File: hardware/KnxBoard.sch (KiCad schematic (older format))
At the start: 10 parts, among them J1 Conn_01x10, J1 SB, J2 KNX, J4 Conn_01x02, SW1 SW

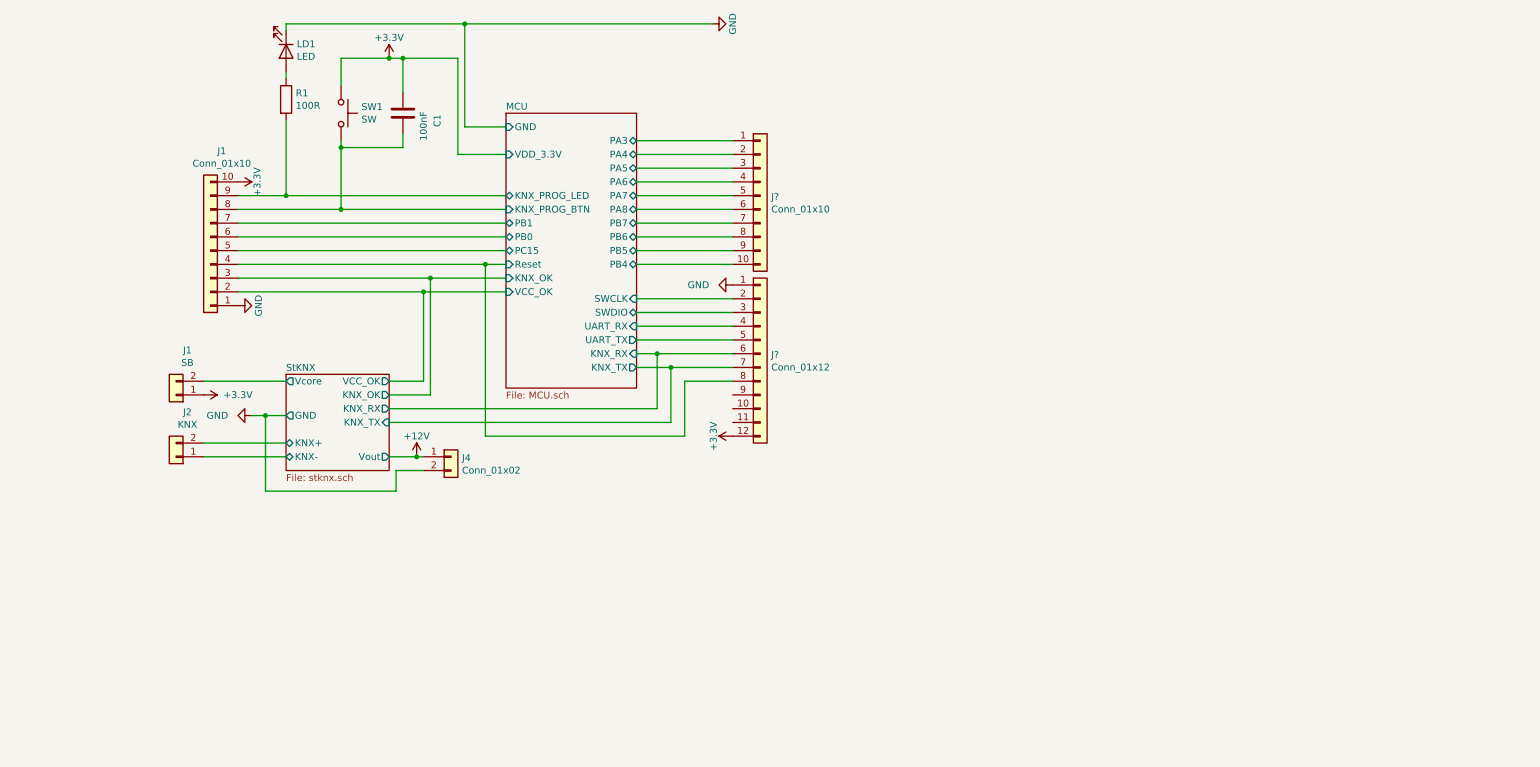
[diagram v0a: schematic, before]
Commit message: Change architecture, use NCN5130 instead STKNX
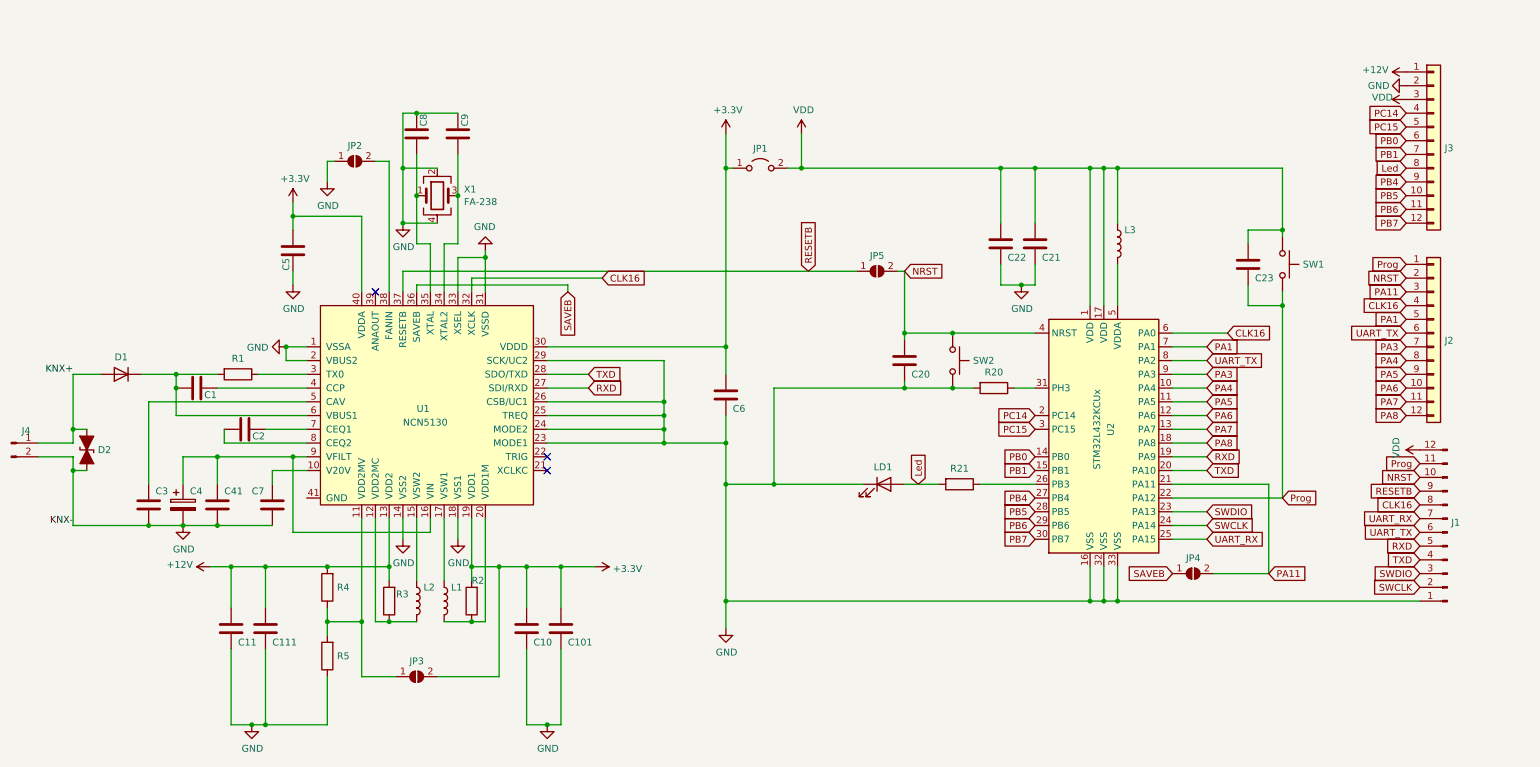
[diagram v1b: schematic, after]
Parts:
- removed J1: SB, Connector_PinHeader_2.54mm:PinHeader_1x02_P2.54mm_Vertical, symbol Connector_Generic:Conn_01x02
- removed J1: Conn_01x10, Connector_PinHeader_2.54mm:PinHeader_1x14_P2.54mm_Vertical, symbol Connector_Generic:Conn_01x10
- removed J2: KNX, stknx:KNX_Connector, symbol Connector_Generic:Conn_01x02
- removed J4: Conn_01x02, Connector_PinHeader_2.54mm:PinHeader_1x02_P2.54mm_Vertical, symbol Connector_Generic:Conn_01x02
- removed J?: Conn_01x12, Connector_FFC-FPC:Hirose_FH12-12S-0.5SH_1x12-1MP_P0.50mm_Horizontal, symbol Connector_Generic:Conn_01x12
- removed J?: Conn_01x10, symbol Connector_Generic:Conn_01x10
- added C10, C101, C11, C111, C22: 10uF 6.3V ESR < 0.1ohm, Capacitor_SMD:C_0805_2012Metric, symbol Device:C
- added C2: 220nF 50V, Capacitor_SMD:C_0603_1608Metric, symbol Device:C
- added C20, C21, C23, C5, C6: 100nF 6.3V, Capacitor_SMD:C_0402_1005Metric, symbol Device:C
- added C3: 100nF 50V, Capacitor_SMD:C_0603_1608Metric, symbol Device:C
- added C4: 100uF 35V, Capacitor_SMD:CP_Elec_6.3x7.7, symbol Device:CP
- added C41, C7: 1uF 35V ESR < 2ohm, Capacitor_SMD:C_0603_1608Metric, symbol Device:C
- added C8, C9: 10pF 6.3V, Capacitor_SMD:C_0402_1005Metric, symbol Device:C
- added D1: SS16, Diode_SMD:D_SMA, symbol Device:D
- added D2: 1SMA40CA, Diode_SMD:D_SMA, symbol Device:D_TVS_ALT
- added J1: Conn_01x12_Male, Connector_FFC-FPC:Hirose_FH12-12S-0.5SH_1x12-1MP_P0.50mm_Horizontal, symbol Connector:Conn_01x12_Male
- added J2, J3: Conn_01x12, Connector_PinHeader_2.54mm:PinHeader_1x12_P2.54mm_Vertical, symbol Connector_Generic:Conn_01x12
- added J4: Conn_01x02_Male, KnxBoard:KNX_Connector, symbol Connector:Conn_01x02_Male
- added JP1: Jumper_2_Open, Connector_PinHeader_2.54mm:PinHeader_1x02_P2.54mm_Vertical, symbol Jumper:Jumper_2_Open
- added JP2, JP3, JP4, JP5: SolderJumper_2_Open, Jumper:SolderJumper-2_P1.3mm_Open_TrianglePad1.0x1.5mm, symbol Jumper:SolderJumper_2_Open
- added L1, L2, L3: 220uH, Inductor_SMD:L_1008_2520Metric, symbol Device:L
- added R2, R3: 1R 1/16W, Resistor_SMD:R_0402_1005Metric, symbol Device:R
- added R20: 10K 1/16w, Resistor_SMD:R_0402_1005Metric, symbol Device:R
- added R21: 100R, Resistor_SMD:R_0402_1005Metric, symbol Device:R
- added R4: 67.7K 1/16w, Resistor_SMD:R_0402_1005Metric, symbol Device:R
- added R5: 590K 1/16w, Resistor_SMD:R_0402_1005Metric, symbol Device:R
- added SW2: SW_Push, Button_Switch_SMD:SW_SPST_SKQG_WithStem, symbol Switch:SW_Push
- added U1: NCN5130, Package_DFN_QFN:QFN-40-1EP_6x6mm_P0.5mm_EP4.6x4.6mm_ThermalVias, symbol KNX_NCN5130:NCN5130
- added U2: STM32L432KCUx, Package_DFN_QFN:QFN-32-1EP_5x5mm_P0.5mm_EP3.45x3.45mm, symbol MCU_ST_STM32L4:STM32L432KCUx
- added X1: FA-238, Crystal:Crystal_SMD_SeikoEpson_FA238-4Pin_3.2x2.5mm, symbol Device:Crystal_GND24
- C1: value 100nF -> 47nF 50V; Price 0.09 -> 0.085; Rating 3.3V -> (none)
- LD1: Price 0.15 -> 0.152
- R1: value 100R -> 27R 1W; footprint Resistor_SMD:R_0402_1005Metric -> Resistor_SMD:R_0612_1632Metric; Price 0.09 -> 0.382
- SW1: value SW -> SW_Push; Price 0.5 -> 0.497
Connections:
- net MCU/KNX_PROG_LED is gone; now on an unnamed net: R1.2
- net +12V: now also C11.1, C111.1, J3.1 (Pin_1), R3.2, R4.2, U1.13 (VDD2)
- net +3V3: now also C10.1, C101.1, C5.2, C6.1, JP1.1 (A), JP3.2 (B), R2.2, U1.19 (VDD1), U1.30 (VDDD), U1.40 (VDDA); no longer C1.1, SW1.1
- net GND: now also C10.2, C101.2, C11.2, C111.2, C20.2, C21.2, C22.2, C3.2, C4.2, C41.2, C5.1, C6.2, C7.2, C8.1, C9.1, D2.2 (A2), J1.1 (Pin_1), J3.2 (Pin_2), J4.2 (Pin_2), JP2.1 (A), R20.2, R5.1, SW2.2, U1.1 (VSSA), U1.14 (VSS2), U1.18 (VSS1), U1.2 (VBUS2), U1.23 (MODE1), U1.24 (MODE2), U1.25 (TREQ), U1.26 (CSB/UC1), U1.29 (SCK/UC2), U1.31 (VSSD), U1.33 (XSEL), U2.16 (VSS), U2.32 (VSS), U2.33 (VSS), X1.2, X1.4
- net at R1.1: now also U1.3 (TX0); no longer LD1.2 (A)
- net MCU/KNX_PROG_BTN: no longer names the net of C1.2
- net MCU/KNX_PROG_BTN: now also D1.1 (K), U1.6 (VBUS1); no longer SW1.2
- new net: R21.1, U2.26 (PB3)
- new net: R20.1, U2.31 (PH3)
- new net: L3.2, U2.5 (VDDA)
- new net: C7.1, U1.10 (V20V)
- new net: JP3.1 (A), R4.1, R5.2, U1.11 (VDD2MV)
- new net: L2.2, R3.1, U1.12 (VDD2MC)
- new net: L2.1, U1.15 (VSW2)
- new net: C4.1, C41.1, U1.16 (VIN), U1.9 (VFILT)
- new net: L1.1, U1.17 (VSW1)
- new net: L1.2, R2.1, U1.20 (VDD1M)
- new net: C9.2, U1.34 (XTAL2), X1.3
- new net: C8.2, U1.35 (XTAL), X1.1
- new net: JP2.2 (B), U1.38 (FANIN)
- new net: C1.1, U1.4 (CCP)
- new net: C3.1, U1.5 (CAV)
- new net: C2.1, U1.7 (CEQ1)
- new net: C2.2, U1.8 (CEQ2)
- new net CLK16: J1.8 (Pin_8), J2.4 (Pin_4), U1.32 (XCLK), U2.6 (PA0)
- new net KNX+: D1.2 (A), D2.1 (A1), J4.1 (Pin_1)
- new net Led: J3.8 (Pin_8), LD1.2 (A), R21.2
- new net NRST: C20.1, J1.10 (Pin_10), J2.2 (Pin_2), JP5.2 (B), SW2.1, U2.4 (NRST)
- new net PA1: J2.5 (Pin_5), U2.7 (PA1)
- new net PA11: J2.3 (Pin_3), JP4.2 (B), U2.21 (PA11)
- new net PA3: J2.7 (Pin_7), U2.9 (PA3)
- new net PA4: J2.8 (Pin_8), U2.10 (PA4)
- new net PA5: J2.9 (Pin_9), U2.11 (PA5)
- new net PA6: J2.10 (Pin_10), U2.12 (PA6)
- new net PA7: J2.11 (Pin_11), U2.13 (PA7)
- new net PA8: J2.12 (Pin_12), U2.18 (PA8)
- new net PB0: J3.6 (Pin_6), U2.14 (PB0)
- new net PB1: J3.7 (Pin_7), U2.15 (PB1)
- new net PB4: J3.9 (Pin_9), U2.27 (PB4)
- new net PB5: J3.10 (Pin_10), U2.28 (PB5)
- new net PB6: J3.11 (Pin_11), U2.29 (PB6)
- new net PB7: J3.12 (Pin_12), U2.30 (PB7)
- new net PC14: J3.4 (Pin_4), U2.2 (PC14)
- new net PC15: J3.5 (Pin_5), U2.3 (PC15)
- new net Prog: C23.2, J1.11 (Pin_11), J2.1 (Pin_1), SW1.2, U2.22 (PA12)
- new net RESETB: J1.9 (Pin_9), JP5.1 (A), U1.37 (RESETB)
- new net RXD: J1.5 (Pin_5), U1.27 (SDI/RXD), U2.19 (PA9)
- new net SAVEB: JP4.1 (A), U1.36 (SAVEB)
- new net SWCLK: J1.2 (Pin_2), U2.24 (PA14)
- new net SWDIO: J1.3 (Pin_3), U2.23 (PA13)
- new net TXD: J1.4 (Pin_4), U1.28 (SDO/TXD), U2.20 (PA10)
- new net UART_RX: J1.7 (Pin_7), U2.25 (PA15)
- new net UART_TX: J1.6 (Pin_6), J2.6 (Pin_6), U2.8 (PA2)
- new net VDD: C21.1, C22.1, C23.1, J1.12 (Pin_12), J3.3 (Pin_3), JP1.2 (B), L3.1, SW1.1, U2.1 (VDD), U2.17 (VDD)
- no-connect marks 0 -> 3

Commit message: KnxBoard: Continue with layer 2
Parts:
- removed C101, C111: 10uF 6.3V ESR < 0.1ohm, Capacitor_SMD:C_0805_2012Metric, symbol Device:C
- removed C7: 1uF 35V ESR < 2ohm, Capacitor_SMD:C_0603_1608Metric, symbol Device:C
- removed J1: Conn_01x12_Male, Connector_FFC-FPC:Hirose_FH12-12S-0.5SH_1x12-1MP_P0.50mm_Horizontal, symbol Connector:Conn_01x12_Male
- removed JP2, JP3, JP4, JP5: SolderJumper_2_Open, Jumper:SolderJumper-2_P1.3mm_Open_TrianglePad1.0x1.5mm, symbol Jumper:SolderJumper_2_Open
- added J1: Conn_01x10, Connector_PinHeader_1.27mm:PinHeader_2x05_P1.27mm_Vertical, symbol Connector_Generic:Conn_01x10
- added R6: NOTMOUNT, Resistor_SMD:R_0603_1608Metric, symbol Device:R
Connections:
- net RESETB is gone; now on net NRST: U1.37 (RESETB)
- net SAVEB is gone; now on net PA11: U1.36 (SAVEB)
- net +3V3: now also U1.21 (XCLKC)
- net GND: now also U1.41 (GND), J1.2 (Pin_2), R6.2
- net NRST: now also J1.3 (Pin_3)
- net RXD: now also J1.9 (Pin_9)
- net SWCLK: now also J1.6 (Pin_6)
- net SWDIO: now also J1.7 (Pin_7)
- net TXD: now also J1.8 (Pin_8)
- net UART_RX: now also J1.4 (Pin_4)
- net UART_TX: now also J1.5 (Pin_5)
- net VDD: now also J1.10 (Pin_10)
- net Vfilt: now reaches U1.10 (V20V)
- net Vfilt: now also C4.1, C41.1, U1.16 (VIN), U1.9 (VFILT)
- net CLK1: now reaches C9.2, U1.34 (XTAL2), X1.3
- net CLK0: now reaches C8.2, U1.35 (XTAL), X1.1
- net at U1.38 (FANIN): now also R6.1
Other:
- moved on the sheet: C11

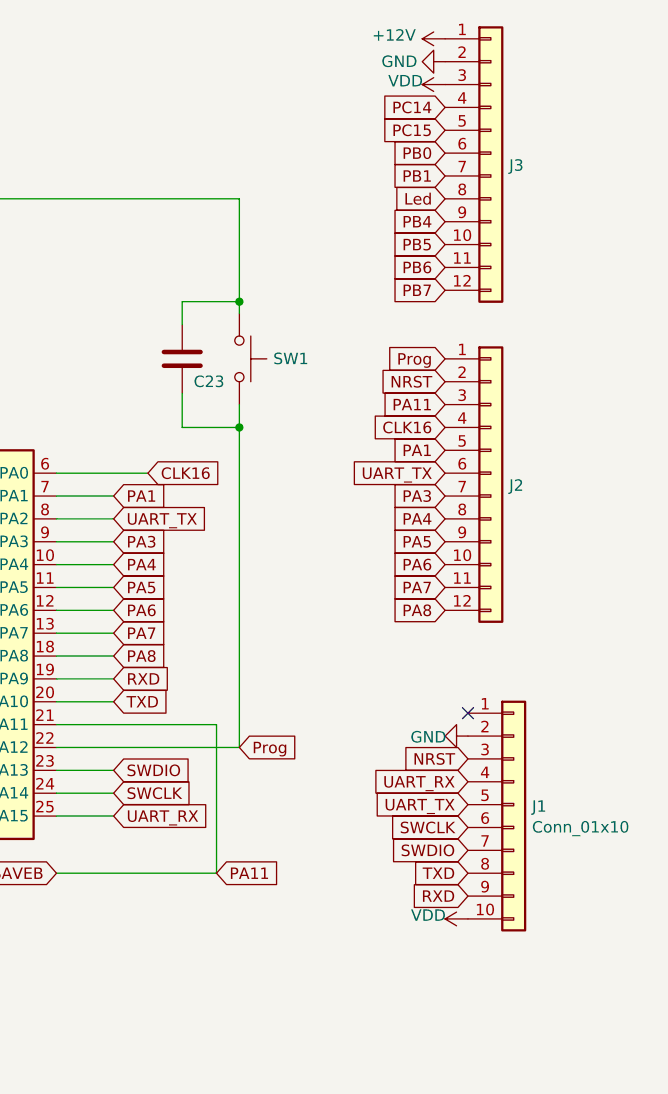
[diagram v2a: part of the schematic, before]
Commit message: Switch into 4-layers
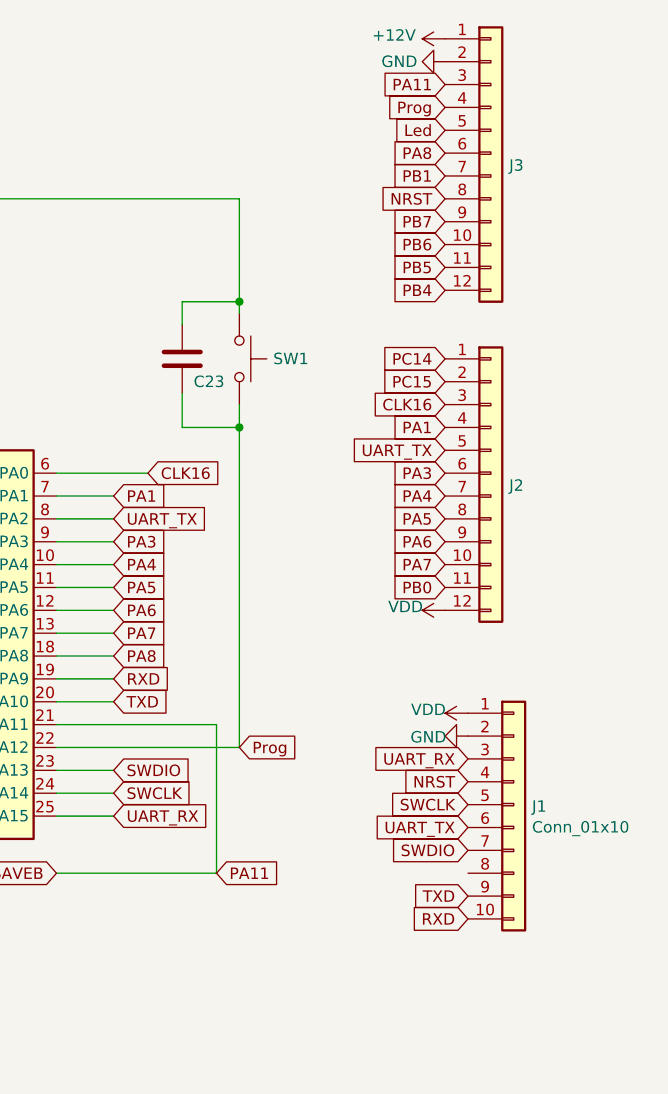
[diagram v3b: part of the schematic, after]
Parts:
- C20, C21, C23, C5, C6, C8, C9: footprint Capacitor_SMD:C_0402_1005Metric -> Capacitor_SMD:C_0603_1608Metric
- R2, R3: footprint Resistor_SMD:R_0402_1005Metric -> Resistor_SMD:R_0603_1608Metric; Price 0.085 -> 0.008
- R20: footprint Resistor_SMD:R_0402_1005Metric -> Resistor_SMD:R_0603_1608Metric
- R21: footprint Resistor_SMD:R_0402_1005Metric -> Resistor_SMD:R_0603_1608Metric; Price 0.085 -> 0.075
- R4: value 67.7K 1/16w -> 56K 1/16w; footprint Resistor_SMD:R_0402_1005Metric -> Resistor_SMD:R_0603_1608Metric; Price 0.229 -> 0.08
- R5: value 590K 1/16w -> 499K 1/16w; footprint Resistor_SMD:R_0402_1005Metric -> Resistor_SMD:R_0603_1608Metric; Price 0.085 -> 0.102
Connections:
- net CLK16: now also J2.3 (Pin_3); no longer J2.4 (Pin_4)
- net Led: now also J3.5 (Pin_5); no longer J3.8 (Pin_8)
- net NRST: now also J1.4 (Pin_4), J3.8 (Pin_8); no longer J1.3 (Pin_3), J2.2 (Pin_2)
- net PA1: now also J2.4 (Pin_4); no longer J2.5 (Pin_5)
- net PA11: now also J3.3 (Pin_3); no longer J2.3 (Pin_3)
- net PA3: now also J2.6 (Pin_6); no longer J2.7 (Pin_7)
- net PA4: now also J2.7 (Pin_7); no longer J2.8 (Pin_8)
- net PA5: now also J2.8 (Pin_8); no longer J2.9 (Pin_9)
- net PA6: now also J2.9 (Pin_9); no longer J2.10 (Pin_10)
- net PA7: now also J2.10 (Pin_10); no longer J2.11 (Pin_11)
- net PA8: now also J3.6 (Pin_6); no longer J2.12 (Pin_12)
- net PB0: now also J2.11 (Pin_11); no longer J3.6 (Pin_6)
- net PB4: now also J3.12 (Pin_12); no longer J3.9 (Pin_9)
- net PB5: now also J3.11 (Pin_11); no longer J3.10 (Pin_10)
- net PB6: now also J3.10 (Pin_10); no longer J3.11 (Pin_11)
- net PB7: now also J3.9 (Pin_9); no longer J3.12 (Pin_12)
- net PC14: now also J2.1 (Pin_1); no longer J3.4 (Pin_4)
- net PC15: now also J2.2 (Pin_2); no longer J3.5 (Pin_5)
- net Prog: now also J3.4 (Pin_4); no longer J2.1 (Pin_1)
- net RXD: now also J1.10 (Pin_10); no longer J1.9 (Pin_9)
- net SWCLK: now also J1.5 (Pin_5); no longer J1.6 (Pin_6)
- net TXD: now also J1.9 (Pin_9); no longer J1.8 (Pin_8)
- net UART_RX: now also J1.3 (Pin_3); no longer J1.4 (Pin_4)
- net UART_TX: now also J1.6 (Pin_6), J2.5 (Pin_5); no longer J1.5 (Pin_5), J2.6 (Pin_6)
- net VDD: now also J1.1 (Pin_1), J2.12 (Pin_12); no longer J1.10 (Pin_10), J3.3 (Pin_3)
- no-connect marks 3 -> 2

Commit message: Fin de routage
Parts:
- added R22: 0, Resistor_SMD:R_0603_1608Metric, symbol Device:R
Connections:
- net NRST: now also R22.1; no longer U1.37 (RESETB)
- net PA11: now also J2.12 (Pin_12); no longer J3.3 (Pin_3)
- net VDD: now also J3.3 (Pin_3); no longer J2.12 (Pin_12)
- new net: R22.2, U1.37 (RESETB)
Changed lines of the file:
@@
 L power:VDD #PWR0121
 U 1 1 619174D7
-P 10750 3500
-F 0 "#PWR0121" H 10750 3350 50  0001 C CNN
-F 1 "VDD" V 10765 3673 50  0000 C CNN
-F 2 "" H 10750 3500 50  0001 C CNN
-F 3 "" H 10750 3500 50  0001 C CNN
-	1    10750 3500
+P 10750 1200
+F 0 "#PWR0121" H 10750 1050 50  0001 C CNN
+F 1 "VDD" V 10765 1373 50  0000 C CNN
+F 2 "" H 10750 1200 50  0001 C CNN
+F 3 "" H 10750 1200 50  0001 C CNN
+	1    10750 1200
 	0    -1   -1   0
 $EndComp
@@
 Connection ~ 2600 4600
 Wire Wire Line
-	3450 2450 7100 2450
+	3450 2450 6250 2450
 Wire Wire Line
 	9050 4100 9850 4100
@@
 	1    0    0    -1
 $EndComp
-Text GLabel 10750 1200 0    50   Input ~ 0
+Text GLabel 10750 3500 0    50   Input ~ 0
 PA11
+$Comp
+L Device:R R22
+U 1 1 6189BABB
+P 6400 2450
+F 0 "R22" V 6285 2450 50  0000 C CNN
+F 1 "0" V 6284 2450 50  0001 C CNN
+F 2 "Resistor_SMD:R_0603_1608Metric" V 6330 2450 50  0001 C CNN
+F 3 "~" H 6400 2450 50  0001 C CNN
+	1    6400 2450
+	0    1    1    0
+$EndComp
+Wire Wire Line
+	6550 2450 7100 2450
 $EndSCHEMATC

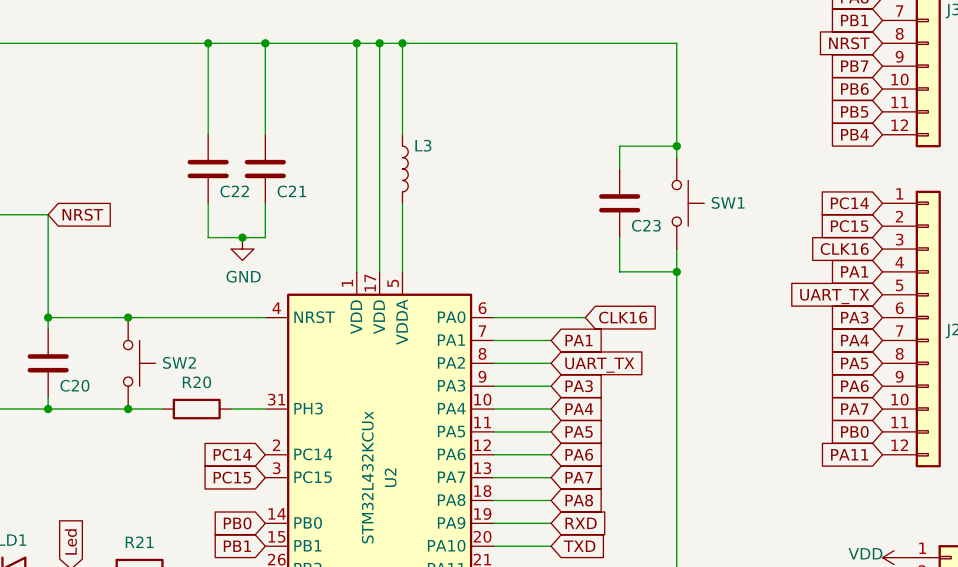
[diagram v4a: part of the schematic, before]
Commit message: Update serigraphie
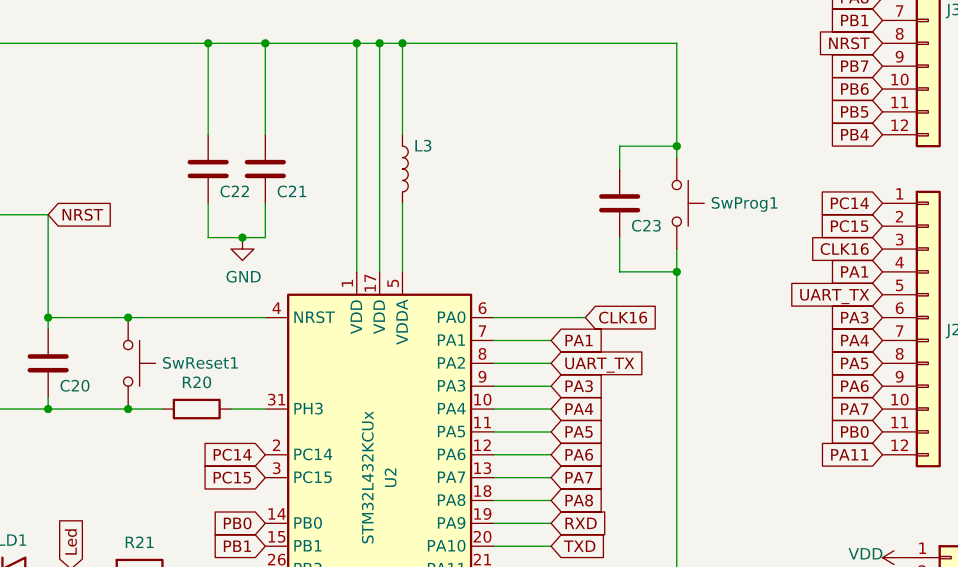
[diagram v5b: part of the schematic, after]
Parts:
- renumbered SW1 to SwProg1, SW2 to SwReset1
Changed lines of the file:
@@
 $EndComp
 $Comp
-L Switch:SW_Push SW2
+L Switch:SW_Push SwReset1
 U 1 1 61933FA8
 P 7450 3100
-F 0 "SW2" V 7450 3248 50  0000 L CNN
+F 0 "SwReset1" V 7450 3248 50  0000 L CNN
 F 1 "SW_Push" V 7495 3248 50  0001 L CNN
 F 2 "Button_Switch_SMD:SW_SPST_SKQG_WithStem" H 7450 3300 50  0001 C CNN
@@
 	6150 4000 5800 4000
 $Comp
-L Switch:SW_Push SW1
+L Switch:SW_Push SwProg1
 U 1 1 619C29D7
 P 9850 2400
-F 0 "SW1" V 9850 2548 50  0000 L CNN
+F 0 "SwProg1" V 9850 2548 50  0000 L CNN
 F 1 "SW_Push" V 9895 2548 50  0001 L CNN
 F 2 "Button_Switch_SMD:SW_SPST_SKQG_WithStem" H 9850 2600 50  0001 C CNN
